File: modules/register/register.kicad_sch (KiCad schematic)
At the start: 30 parts, among them K0 4PDT, K1 4PDT, K2 4PDT, K3 4PDT

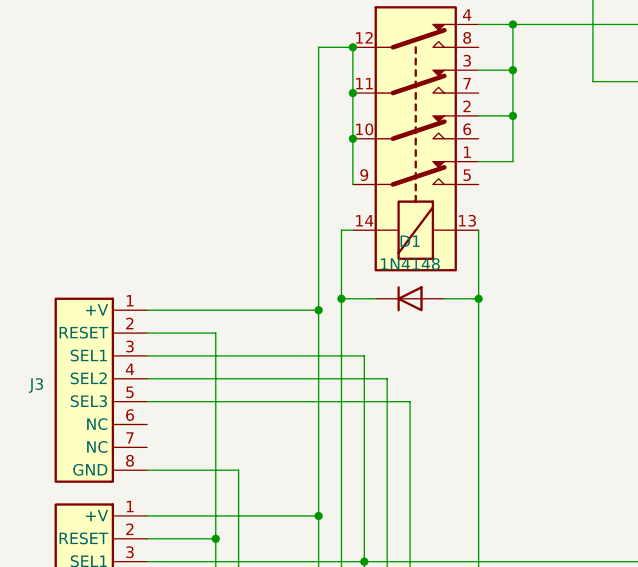
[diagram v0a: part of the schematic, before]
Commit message: Added some modules
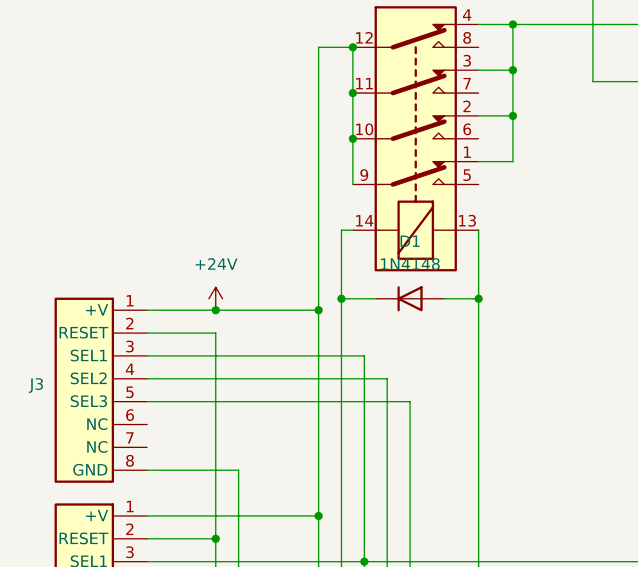
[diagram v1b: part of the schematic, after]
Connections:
- net +24V: now reaches BITS0-3.1 (+V), BITS2-3.1 (+V), BUS1-1.1 (+V), BUS1-2.1 (+V), BUS1-3.1 (+V), BUS2-1.1 (+V), BUS2-2.1 (+V), BUS2-3.1 (+V), BUS3-1.1 (+V), BUS3-2.1 (+V), BUS3-3.1 (+V), J1.1 (+V), J2.1 (+V), J3.1 (+V), K-RESET1.10, K-RESET1.11, K-RESET1.12, K-RESET1.9
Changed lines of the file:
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@@
 	)
 	(junction
+		(at 46.99 123.19)
+		(diameter 0)
+		(color 0 0 0 0)
+	)
+	(junction
 		(at 290.83 184.15)
 		(diameter 0)
@@
 	(wire
 		(pts
-			(xy 39.37 123.19) (xy 58.42 123.19)
+			(xy 39.37 123.19) (xy 46.99 123.19)
 		)
 		(stroke
@@
 	(wire
 		(pts
+			(xy 46.99 123.19) (xy 58.42 123.19)
+		)
+		(stroke
+			(width 0)
+			(type default)
+		)
+	)
+	(wire
+		(pts
 			(xy 153.67 72.39) (xy 158.75 72.39)
 		)
@@
 					(unit 1)
 				)
+			)
+		)
+	)
+	(symbol
+		(lib_id "power:+24V")
+		(at 46.99 123.19 0)
+		(unit 1)
+		(exclude_from_sim no)
+		(in_bom yes)
+		(on_board yes)
+		(dnp no)
+		(fields_autoplaced yes)
+		(property "Reference" "#PWR02"
+			(at 46.99 127 0)
+			(effects
+				(font
+					(size 1.27 1.27)
+				)
+				(hide yes)
+			)
+		)
+		(property "Value" "+24V"
+			(at 46.99 118.11 0)
+			(effects
+				(font
+					(size 1.27 1.27)
+				)
+			)
+		)
+		(property "Footprint" ""
+			(at 46.99 123.19 0)
+			(effects
+				(font
+					(size 1.27 1.27)
+				)
+				(hide yes)
+			)
+		)
+		(property "Datasheet" ""
+			(at 46.99 123.19 0)
+			(effects
+				(font
+					(size 1.27 1.27)
+				)
+				(hide yes)
+			)
+		)
+		(property "Description" "Power symbol creates a global label with name \"+24V\""
+			(at 46.99 123.19 0)
+			(effects
+				(font
+					(size 1.27 1.27)
+				)
+				(hide yes)
+			)
+		)
+		(pin "1"
+		)
+		(instances
+			(project ""
+				(path "/bead2d35-1e2f-4816-978b-a8db64d5e2fc"
+					(reference "#PWR02")
+					(unit 1)
+				)
